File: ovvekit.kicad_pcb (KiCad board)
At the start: 4 copper layers, 75 x 76 mm, 132 parts, among them IC1 MAX4466EXK+T, J1 ESP_PROG_JTAG, J2 ESP_PROG_UART, J201 Power_Planes, Q201 Q_PMOS_GSD, SW1 SW_Push, SW2 SW_Push, SW3 SW_Push, SW4 SW_Push, U1 ESP32-WROOM-32, U201 AP2112K-3.3, U202 LSM6DS3, U203 AMS1117-3.3

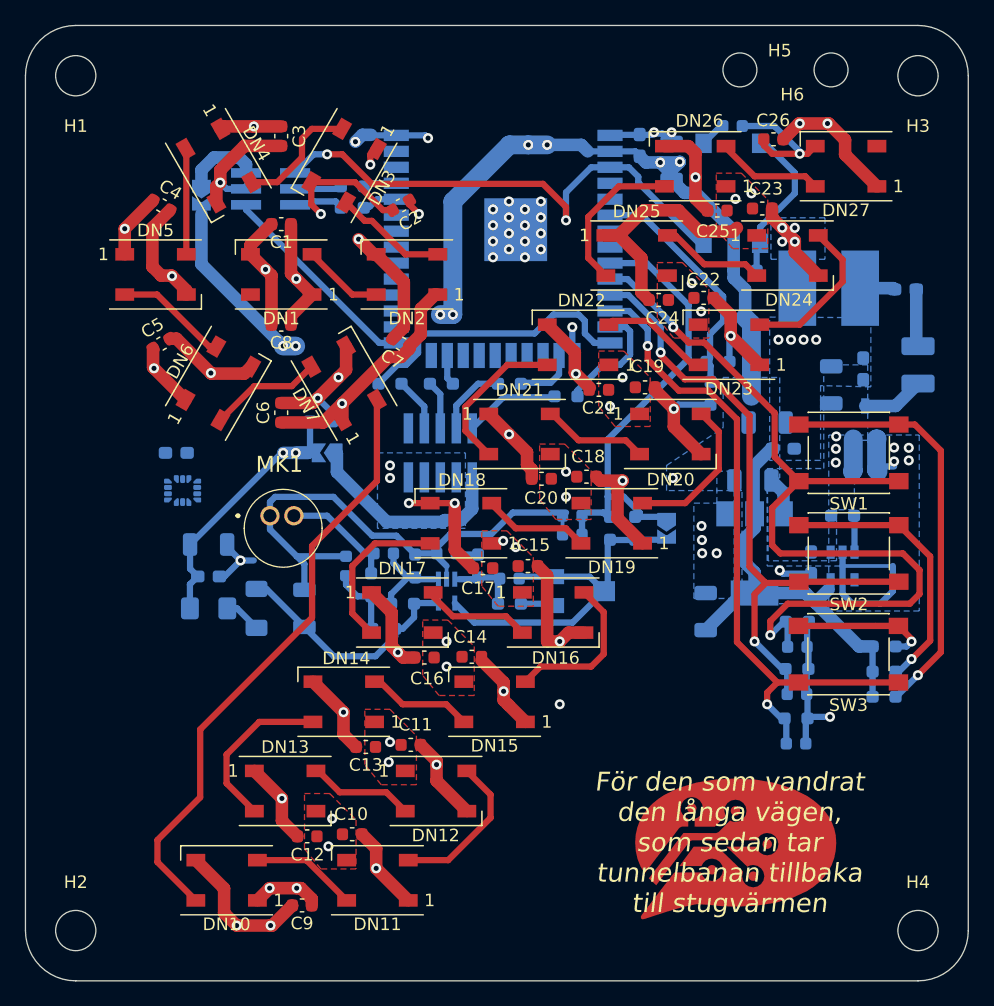
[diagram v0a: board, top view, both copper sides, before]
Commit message: Conected up the last nets.
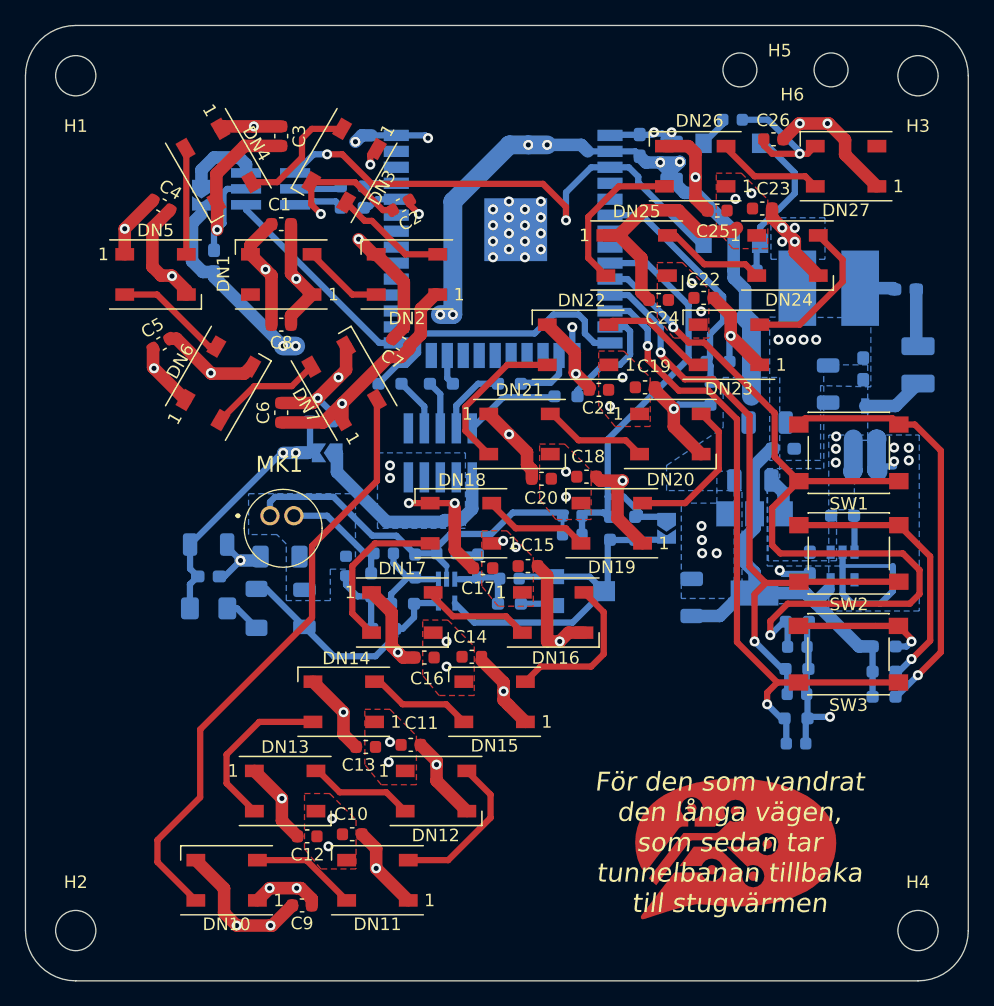
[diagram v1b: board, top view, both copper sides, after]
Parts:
- removed U202: LSM6DS3, Package_LGA:LGA-14_3x2.5mm_P0.5mm_LayoutBorder3x4y
- added R211: 0, Resistor_SMD:R_1206_3216Metric_Pad1.30x1.75mm_HandSolder, B.Cu at (-5.75, 35.2)
- R101, R103, R105, R111: value 220R -> 10k
- moved C31 15.5 mm to (-11.0, 11.8), turned to 90 degrees
- moved C213 1.58 mm to (27.0, 38.5)
- moved C110 0.50 mm to (30.2, 0.50)
- moved C201 0.26 mm to (37.9, 21.5)
- moved C211 0.10 mm to (36.4, 35.8)
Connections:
- J2 pad 1: EN -> RESET
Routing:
- net +3V3: track 149.1 -> 129.1 mm, vias 12 -> 10
- net GNDA: track 43.2 -> 32.2 mm
- net GND: track 210.2 -> 217.1 mm
- added copper zone on B.Cu, net GNDA

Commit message: Added more logos!
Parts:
- added svg2mod: G001, SymbolsOST:admittansen_8mm_SilkScreen, F.Cu at (8.75, -0.25)
- added svg2mod: G***, SymbolsOST:bubbla_8mm_SilkScreen, F.Cu at (17.8, -0.75)
- added svg2mod: G***, SymbolsOST:bubbla_16mm_SilkScreen, B.Cu at (17.0, 51.0)
- svg2mod: value G*** -> G001; footprint SymbolsOST:OST-Logo_20mm_SilkScreen -> SymbolsOST:admittansen_16mm_SilkScreen
- moved svg2mod 11.9 mm to (-5.25, 52.8)
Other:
- board text added: "Ovveskylt v1.0"

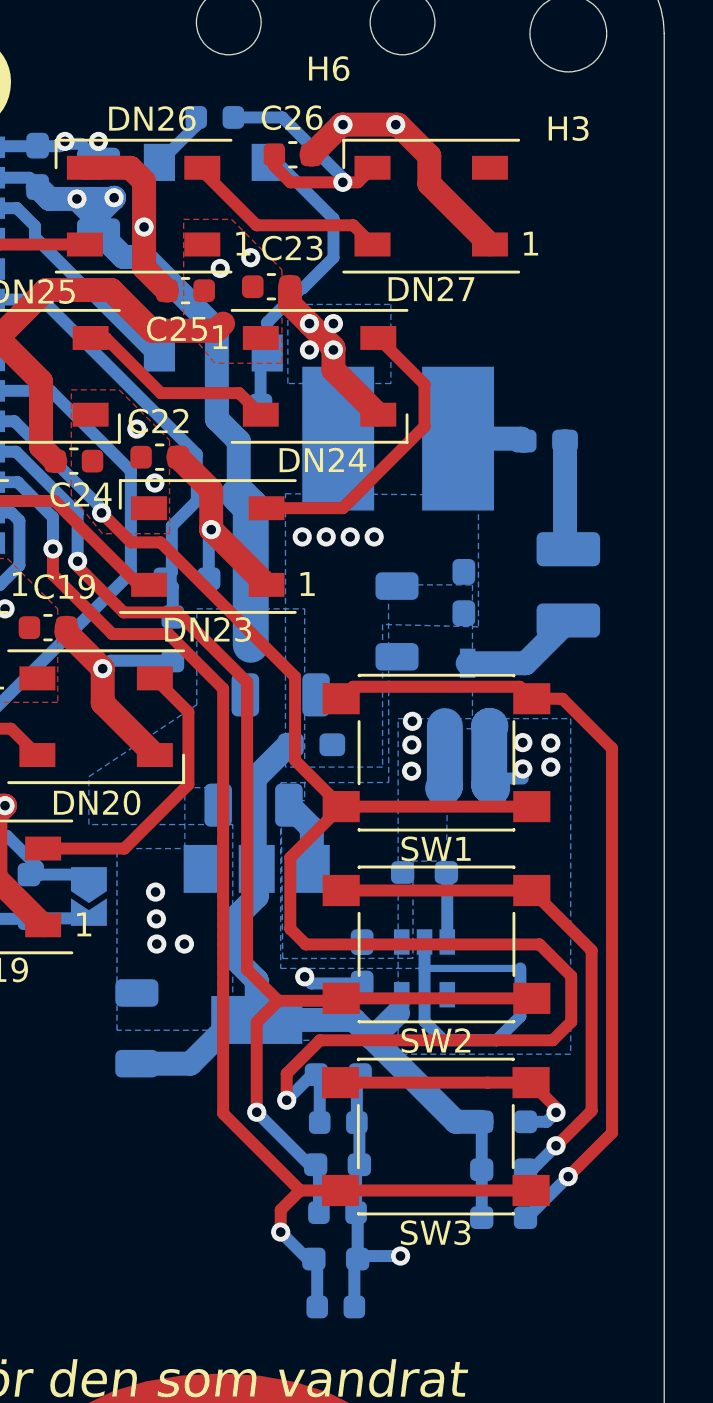
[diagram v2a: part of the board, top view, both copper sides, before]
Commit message: Updated all but polyfuse and ferride bead to correct footprints.
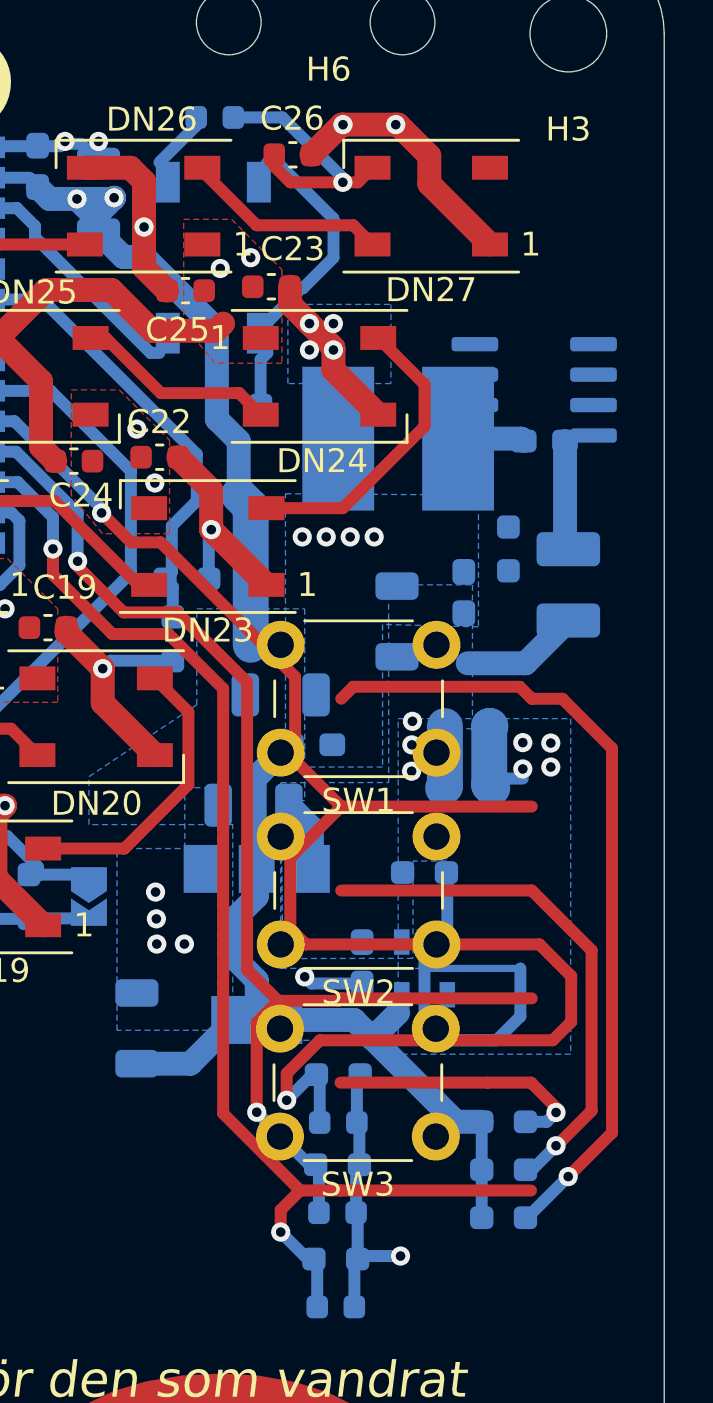
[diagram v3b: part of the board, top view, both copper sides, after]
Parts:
- added R204: 100R, Resistor_SMD:R_0603_1608Metric_Pad0.98x0.95mm_HandSolder, B.Cu at (42.5, 18.5)
- D201: value D_Zener -> BZX284-C5V1; footprint Diode_SMD:D_0805_2012Metric_Pad1.15x1.40mm_HandSolder -> Diode_SMD:D_SOD-110
- Q201: value Q_PMOS_GSD -> SI4435DY_GSD; footprint Package_TO_SOT_SMD:TSOT-23 -> Package_SO:SOIC-8_3.9x4.9mm_P1.27mm
- SW1, SW2, SW3: footprint Button_Switch_SMD:SW_Push_1P1T_NO_6x6mm_H9.5mm -> Button_Switch_THT:SW_PUSH_6mm_H5mm
- SW4: footprint Button_Switch_SMD:SW_Push_1P1T_NO_6x6mm_H9.5mm -> Button_Switch_SMD:SW_SPST_TL3342
- moved Q201 13.0 mm to (43.6, 11.9), turned to 180 degrees
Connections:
- D201 pad 2: GND -> Net-(D201-Pad2)
- Q201 pad 1: GND -> Net-(D201-Pad2)
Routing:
- net +3V3: track 129.1 -> 323.2 mm, vias 10 -> 16
- net BTN_1: track 69.8 -> 3.19 mm
- net BTN_3: track 52.9 -> 0.00 mm, vias 2 -> 0
- net BTN_2: track 51.3 -> 0.00 mm, vias 2 -> 0
- net GND: track 217.1 -> 198.9 mm, vias 69 -> 67
- net VCC: track 139.6 -> 133.3 mm, vias 29 -> 27
- net Net-(D201-Pad2): track 0.00 -> 4.13 mm, vias 0 -> 2
- net Net-(R220-Pad2): track 2.92 -> 0.00 mm

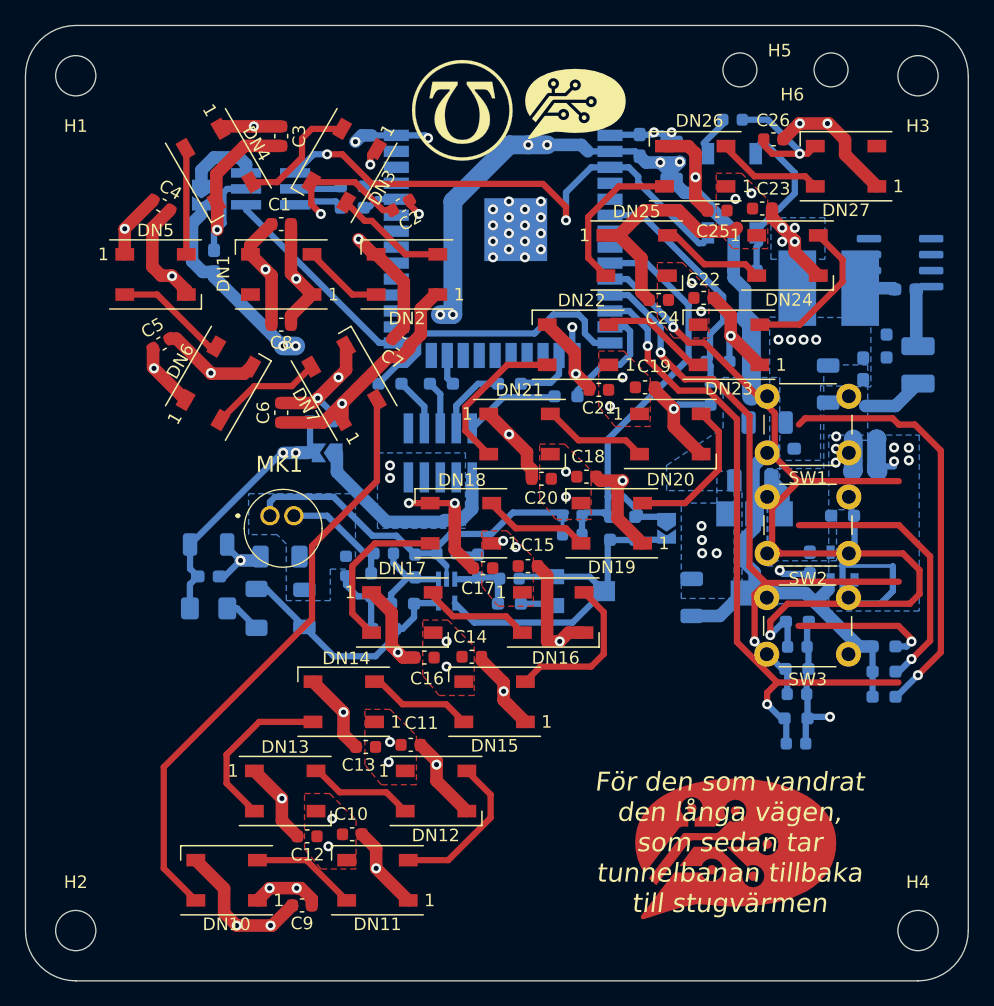
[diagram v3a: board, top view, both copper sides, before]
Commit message: Merged changes from both computers. Moved some components. Next i redoing power section again...
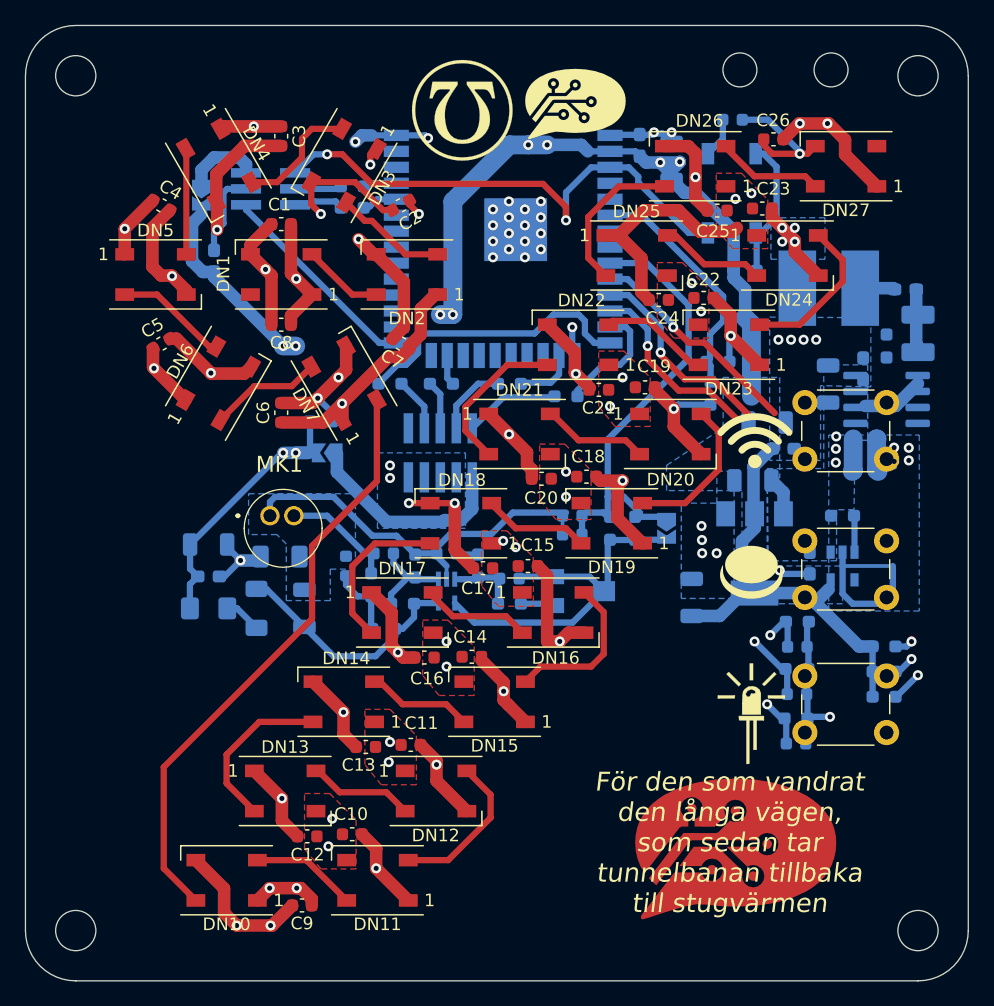
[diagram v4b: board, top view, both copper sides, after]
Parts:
- added button_6mm_SilkScreen: G***, SymbolsOST:button_5mm_SilkScreen, F.Cu at (31.8, 36.5)
- added led_12mm_SilkScreen: G***, SymbolsOST:led_8mm_SilkScreen, F.Cu at (31.8, 47.8)
- added wifi_8mm_SilkScreen: G***, SymbolsOST:wifi_6mm_SilkScreen, F.Cu at (32.0, 26.0)
- moved Q201 10.9 mm to (42.5, 22.8), turned to 0 degrees
- moved SW1 5.32 mm to (36.0, 23.0), turned to 0 degrees
- moved SW3 3.88 mm to (36.0, 44.8), turned to 0 degrees
- moved SW2 3.64 mm to (36.0, 34.0), turned to 0 degrees
- moved F201 2.50 mm to (45.0, 17.5)
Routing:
- net +3V3: track 323.2 -> 143.2 mm, vias 16 -> 10
- net Net-(R101-Pad2): track 33.7 -> 2.49 mm
- net BTN_1: track 3.19 -> 26.3 mm, vias 2 -> 4
- net BTN_2: track 0.00 -> 21.8 mm, vias 0 -> 2
- net Net-(R103-Pad2): track 22.0 -> 1.71 mm
- net BTN_3: track 0.00 -> 19.0 mm, vias 0 -> 2
- net Net-(R105-Pad2): track 11.1 -> 1.64 mm
- net VCC: track 133.3 -> 139.6 mm
- net Net-(F201-Pad2): track 4.94 -> 0.00 mm
- net Net-(R220-Pad2): track 0.00 -> 2.92 mm
- net Net-(R111-Pad2): track 12.8 -> 11.3 mm
- net RESET: track 44.2 -> 44.9 mm

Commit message: Updated power section. Updated all possible footprints to be "hand solder" version. Updated Symbol lib.
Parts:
- removed button_6mm_SilkScreen: G***, SymbolsOST:button_5mm_SilkScreen
- removed the led_12mm_SilkScreen at (31.8, 47.8)
- removed wifi_8mm_SilkScreen: G***, SymbolsOST:wifi_6mm_SilkScreen
- added button_5mm_SilkScreen: G***, SymbolsOST:button_6mm_SilkScreen, F.Cu at (31.8, 47.0)
- added led_12mm_SilkScreen: G***, SymbolsOST:led_12mm_SilkScreen, F.Cu at (31.5, 38.0)
- added wifi_5mm_SilkScreen: G***, SymbolsOST:wifi_6mm_SilkScreen, F.Cu at (39.0, 18.8)
- C1, C10, C100, C101, C102, C11, C110, C12, C13, C14, C15, C16, C17, C18, C19, C2, C20, C21, C22, C23, C24, C25, C26, C27, C28, C29, C3, C30, C310, C311, C4, C5, C6, C7, C8, C9: footprint Capacitor_SMD:C_0603_1608Metric -> Capacitor_SMD:C_0603_1608Metric_Pad1.08x0.95mm_HandSolder
- C201, C202, C203, C208, C209, C212, C213: footprint Capacitor_SMD:C_1206_3216Metric -> Capacitor_SMD:C_1206_3216Metric_Pad1.33x1.80mm_HandSolder
- FB1: footprint Capacitor_SMD:C_0603_1608Metric_Pad1.08x0.95mm_HandSolder -> Capacitor_SMD:C_1206_3216Metric_Pad1.33x1.80mm_HandSolder
- moved C202 19.7 mm to (38.0, 5.50), turned to -90 degrees
- moved C213 19.1 mm to (30.5, 19.8), turned to 0 degrees
- moved FB1 17.9 mm to (30.2, 25.5), turned to 90 degrees
- moved R220 17.3 mm to (24.7, 41.7)
- moved R101 16.9 mm to (37.2, 30.2)
- moved C100 16.4 mm to (39.5, 26.5)
- moved R102 16.4 mm to (39.5, 24.5)
- moved C211 14.8 mm to (22.0, 39.4), turned to 90 degrees
- moved U201 14.5 mm to (24.7, 38.5), turned to 0 degrees
- moved R103 12.9 mm to (42.0, 31.5)
- moved C210 12.6 mm to (33.5, 30.8)
- moved R105 12.4 mm to (42.0, 30.0)
- moved F201 10.9 mm to (42.2, 7.00), turned to 0 degrees
- moved D201 10.5 mm to (40.5, 18.0), turned to 180 degrees
- moved R111 10.4 mm to (27.8, 2.75), turned to 90 degrees
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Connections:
- C202 pad 1: +3V3 -> GND
- C202 pad 2: GND -> Net-(F201-Pad1)
- FB1 pad 2: Net-(F201-Pad1) -> +3V3
- J201 pad 1: Net-(FB1-Pad1) -> Net-(F201-Pad1)
- U201 pad 5: +3V3 -> Net-(FB1-Pad1)
- U203 pad 2: +3V3 -> Net-(FB1-Pad1)
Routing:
- net BTN_3: track 19.0 -> 56.1 mm, vias 2 -> 1
- net +3V3: track 143.2 -> 106.1 mm
- net Net-(R105-Pad2): track 1.64 -> 27.9 mm, vias 1 -> 0
- net BTN_2: track 21.8 -> 44.6 mm, vias 2 -> 1
- net Net-(FB1-Pad1): track 2.78 -> 22.2 mm
- net AUDIO_OUT: track 36.6 -> 21.1 mm
- net Net-(R103-Pad2): track 1.71 -> 14.8 mm, vias 1 -> 0
- net BTN_1: track 26.3 -> 35.3 mm, vias 4 -> 1
- net Net-(C30-Pad1): track 29.7 -> 20.8 mm
- net Net-(R101-Pad2): track 2.49 -> 10.1 mm, vias 1 -> 0
- net RESET: track 44.9 -> 38.4 mm
- net Battery_monitor: track 19.1 -> 24.0 mm
- net VCC: track 139.6 -> 134.9 mm, vias 27 -> 37
- net Net-(F201-Pad1): track 4.57 -> 0.00 mm
- net Net-(R220-Pad2): track 2.92 -> 5.56 mm
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- added copper zone on B.Cu, net AUDIO_OUT
- added copper zone on B.Cu, net Net-(C30-Pad1)
- added copper zone on B.Cu, net Net-(F201-Pad1)
- added copper zone on B.Cu, net Net-(F201-Pad2)
